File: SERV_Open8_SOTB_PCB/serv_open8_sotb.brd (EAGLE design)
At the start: 138.5 x 140 mm, 158 parts, among them IC1 TPS76201DBVR, IC12 SN74LVC1GU04DBVR, IC13 SN74LVC1GU04DBVR, IC2 TPS76201DBVR, IC5 TPS76201DBVR, IC7 TPS76201DBVR, IC8 TPS76201DBVR, IC9 TPS76201DBVR, Q1 BSH103,235, Q10 BSH103,235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

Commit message: Add files via upload
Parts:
- moved GND 6.00 mm to (-42.0, 6.50)
- moved VBP 0.50 mm to (45.0, -11.5)
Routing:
- net GND: track 881.3 -> 887.1 mm
- net DR_VDD: track 153.8 -> 153.3 mm
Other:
- board text added: "0"
- board text added: "CLOCK"
- board text added: "FLASH"
- board text added: "JTAG"
- board text added: "LoRa"
- board text added: "POWER"
- board text added: "POWER LEDs"
- board text added: "SPI"
- board text added: "UART"

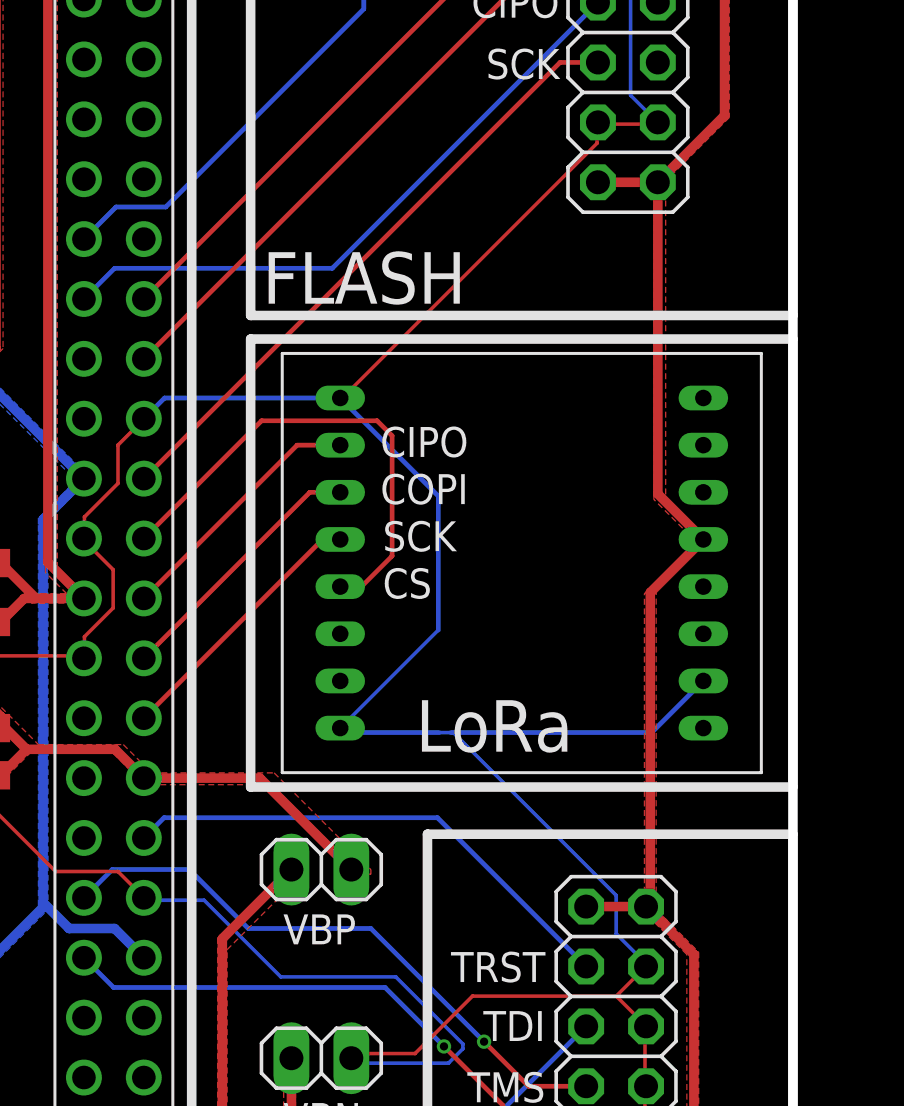
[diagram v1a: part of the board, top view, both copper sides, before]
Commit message: Update new footprint for Lora module
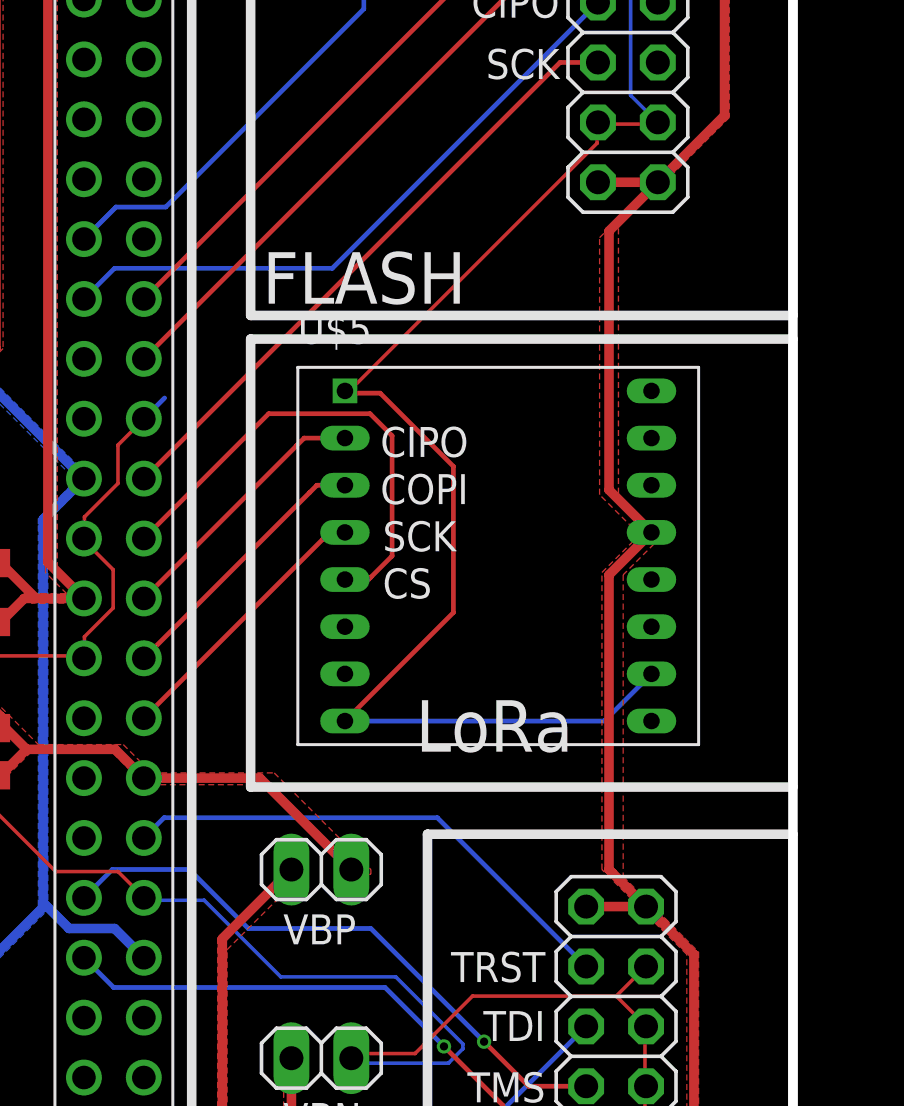
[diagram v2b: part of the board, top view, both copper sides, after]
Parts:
- removed LORA_MODULE: (no value), qfp160:RFM95-915S2
- added U$5: (no value), Duy:RFM95W-915S2
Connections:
- net DR_ALL_I_SPI_CIPO: now also U$5.P$2; no longer LORA_MODULE.P$2
- net DR_ALL_O_SPI_COPI: now also U$5.P$3; no longer LORA_MODULE.P$3
- net DR_ALL_O_SPI_CS: now also U$5.P$5; no longer LORA_MODULE.P$5
- net DR_ALL_O_SPI_SCK: now also U$5.P$4; no longer LORA_MODULE.P$4
- net GND: now also U$5.P$1, U$5.P$15, U$5.P$8; no longer LORA_MODULE.P$1, LORA_MODULE.P$15, LORA_MODULE.P$8
- net VDD_3V3: now also U$5.P$12; no longer LORA_MODULE.P$12
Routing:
- net GND: track 887.1 -> 864.5 mm
- net VDD_3V3: track 759.4 -> 760.5 mm

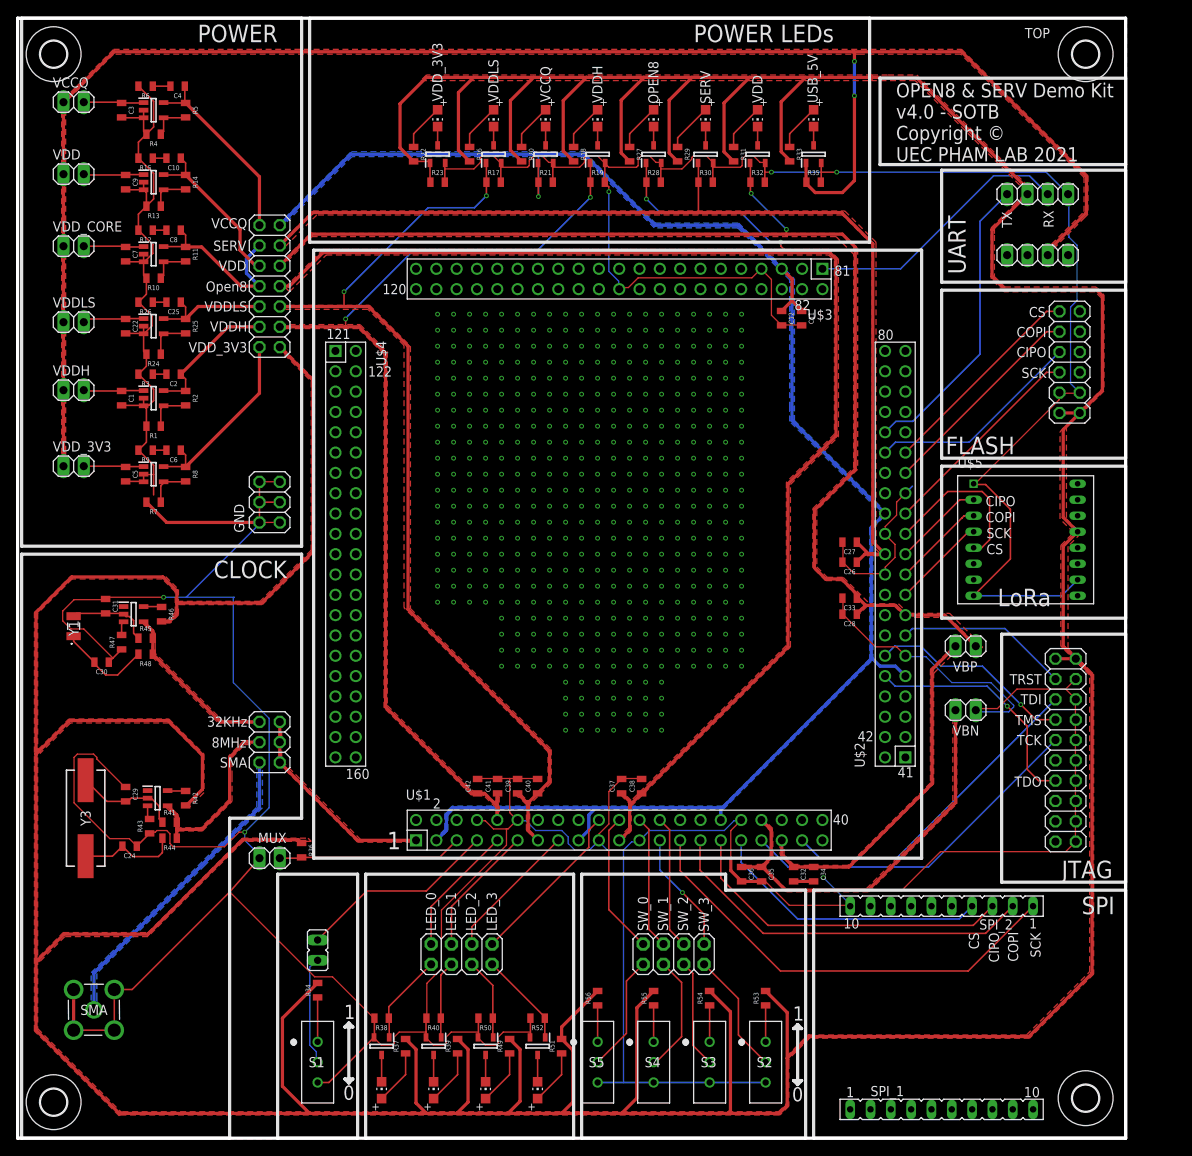
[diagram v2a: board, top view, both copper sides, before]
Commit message: Update new regulators
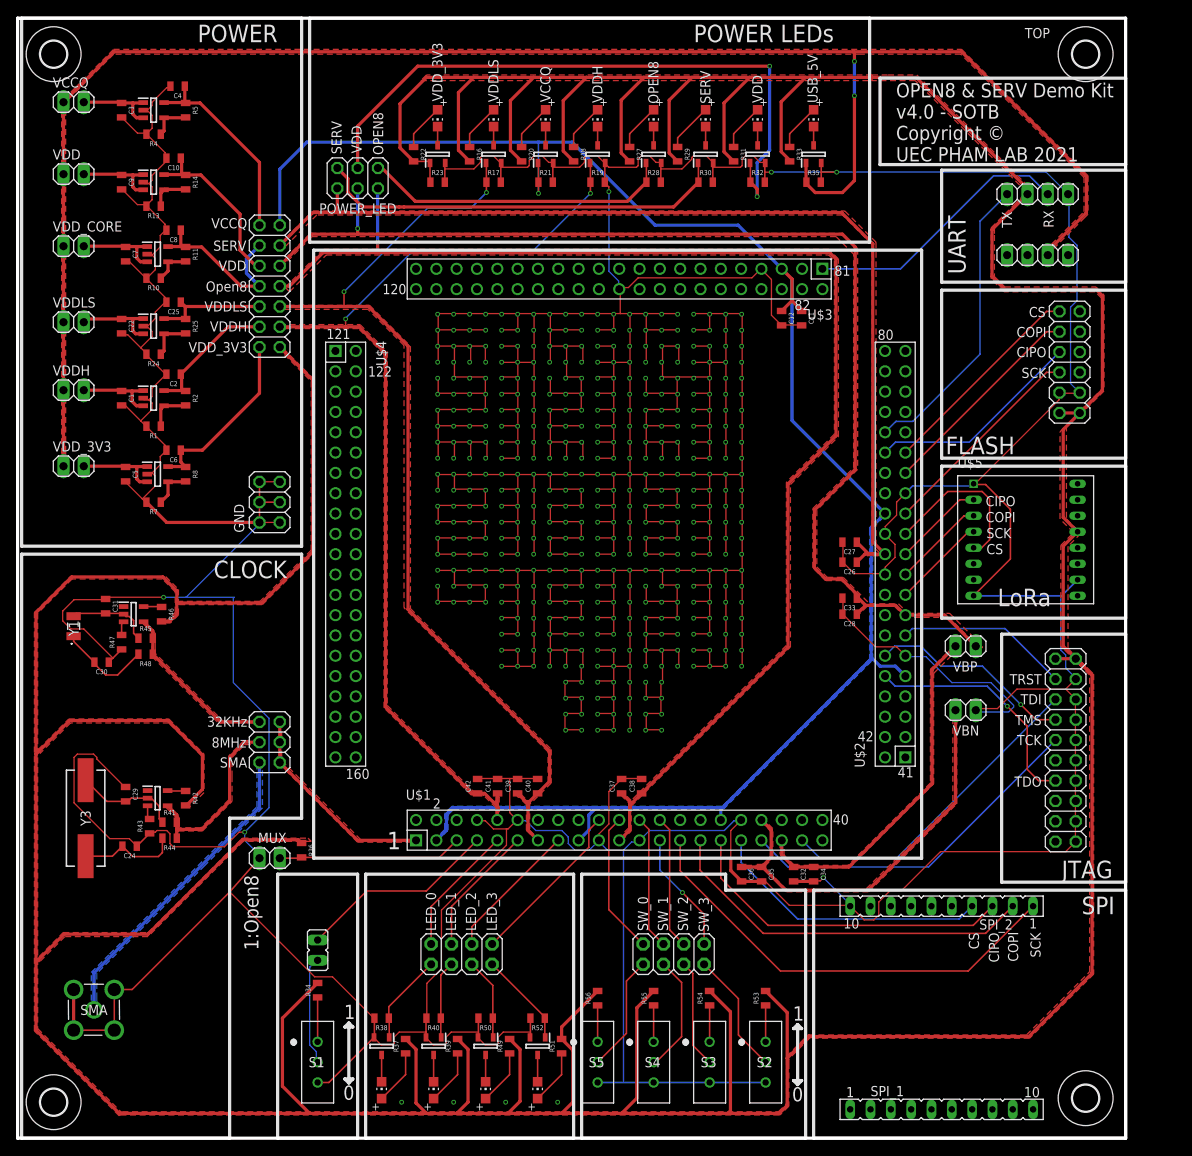
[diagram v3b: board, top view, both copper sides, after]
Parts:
- removed R12, R15, R26, R3, R6, R9: 1, SparkFun-Resistors:0805
- added POWER_LED: PINHD-2X3, Connector:2X03
- IC1, IC2, IC5, IC7, IC8, IC9: value TPS76201DBVR -> AP7331-WG-7; device SamacSys_Parts:SOT95P280X145-5N -> SamacSys_Parts:SOT95P285X145-5N
- R11, R14, R2: value 53.6k -> 133k
- R25: value 3.3k -> 66.5k
- R5, R8: value 243k -> 482k
- moved C22 0.50 mm to (-60.5, 28.5)
- moved C9 0.50 mm to (-60.5, 46.5)
- moved IC7 0.50 mm to (-56.0, 10.0)
- moved IC8 0.50 mm to (-56.0, 37.5)
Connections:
- removed net N$12: C10.2, R15.1
- removed net N$19: C25.2, R26.1
- removed net N$2: C2.2, R3.1
- removed net N$4: C4.2, R6.1
- removed net N$6: C6.2, R9.1
- removed net N$8: C8.2, R12.1
- new net DR_OPEN8_VDD_LED: POWER_LED.6, Q5.1, R28.1
- new net DR_SERV_VDD_LED: POWER_LED.2, Q6.1, R30.1
- new net DR_VDD_LED: POWER_LED.4, Q7.1, R32.1
- net DR_OPEN8_VDD: now also POWER_LED.5; no longer Q5.1, R28.1
- net DR_SERV_VDD: now also POWER_LED.1; no longer Q6.1, R30.1
- net DR_VDD: now also POWER_LED.3; no longer Q7.1, R32.1
- net GND: now also C10.2, C2.2, C25.2, C4.2, C6.2, C8.2; no longer IC1.3, IC2.3, IC5.3, IC7.3, IC8.3, IC9.3, R12.2, R15.2, R26.2, R3.2, R6.2, R9.2
- net IN_VDD: now also IC9.3
- net IN_VDDH: now also IC2.3
- net IN_VDDLS: now also IC1.3
- net IN_VDDQ: now also IC5.3
- net IN_VDD_3V3: now also IC7.3
- net IN_VDD_CORE: now also IC8.3
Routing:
- net GND: track 864.5 -> 1859.3 mm, vias 478 -> 482
- net DR_VDD_LED: track 0.00 -> 81.4 mm, vias 0 -> 2
- net DR_SERV_VDD_LED: track 0.00 -> 51.9 mm
- net DR_OPEN8_VDD_LED: track 0.00 -> 38.7 mm
- net DR_OPEN8_VDD: track 182.6 -> 165.5 mm, vias 2 -> 1
- net VCCQ: track 221.6 -> 227.7 mm
- net DR_VDD: track 153.3 -> 148.3 mm, vias 2 -> 1
- net IN_VDD_3V3: track 7.57 -> 11.0 mm
- net IN_VDD_CORE: track 7.54 -> 10.9 mm
- net DR_SERV_VDD: track 129.2 -> 126.0 mm
- net IN_VDDLS: track 7.67 -> 10.6 mm
- net IN_VDD: track 7.54 -> 10.4 mm
- net IN_VDDH: track 7.54 -> 10.4 mm
- net IN_VDDQ: track 7.54 -> 10.4 mm
- net N$4: track 2.20 -> 0.00 mm
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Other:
- board text added: "1:Open8"
